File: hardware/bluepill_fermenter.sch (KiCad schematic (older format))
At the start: 1 part, among them J1 Conn_01x02

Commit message: Differentail control
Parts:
- added C1, C2, C3, C4: 100nF, symbol Device:C
- added J2: Conn_01x07, SIP7, symbol Connector_Generic:Conn_01x07
- added J3: Conn_01x03, symbol Connector_Generic:Conn_01x03
- added J4, J5: Conn_01x04, SIP4, symbol Connector_Generic:Conn_01x04
- added Q1, Q2: 2N7000, Package_TO_SOT_THT:TO-92_Inline, symbol Transistor_FET:2N7000
- added R1, R2: 1K, symbol Device:R
- added R10, R3, R4, R5, R6, R7, R8: 10K, symbol Device:R
- added R11, R12: 470R, symbol Device:R
- added R9: 50R, symbol Device:R
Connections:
- net +5V: now also J2.1 (Pin_1), J3.1 (Pin_1), R10.2
- net Bluepill Node/I2C1_SCL: now also J5.3 (Pin_3)
- net Bluepill Node/I2C1_SDA: now also J5.4 (Pin_4)
- net Bluepill Node/UART1_RX: now also J4.3 (Pin_3)
- net Bluepill Node/UART1_TX: now also J4.4 (Pin_4)
- net GNDREF: now also C1.2, C2.2, C3.1, C3.2, J2.7 (Pin_7), J4.2 (Pin_2), J5.2 (Pin_2), R5.1, R6.1, R9.2
- new net: Q1.2 (G), R1.1, R3.2
- new net: Q2.2 (G), R2.1, R4.2
- new net +3V3: J4.1 (Pin_1), J5.1 (Pin_1)
- new net COOLER_CONTROL: R1.2
- new net COOLER_INPUT: J2.5 (Pin_5), R10.1, R7.1
- new net COOLER_LED: J3.2 (Pin_2), R11.1
- new net COOLER_OUTPUT: J2.2 (Pin_2), Q1.3 (D), R11.2
- new net GNDPWR: C4.1, C4.2, J2.4 (Pin_4), Q1.1 (S), Q2.1 (S), R3.1, R4.1, R9.1
- new net HEATER_CONTROL: R2.2
- new net HEATER_INPUT: J2.6 (Pin_6), R8.1
- new net HEATER_LED: J3.3 (Pin_3), R12.1
- new net HEATER_OUTPUT: J2.3 (Pin_3), Q2.3 (D), R12.2
- new net TEMP0: C1.1, R5.2, R7.2
- new net TEMP1: C2.1, R6.2, R8.2

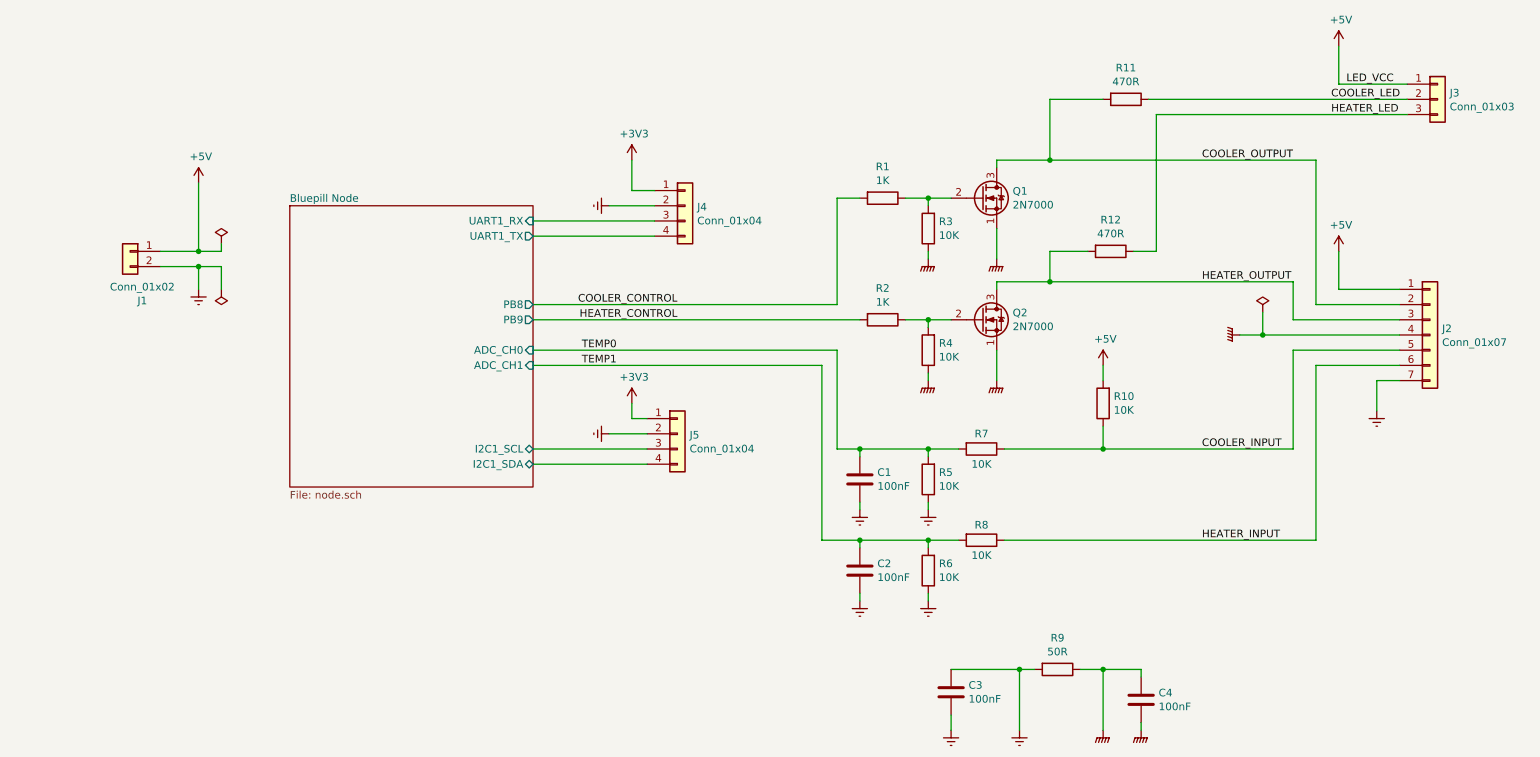
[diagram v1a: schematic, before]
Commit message: Add onboard temp sensor
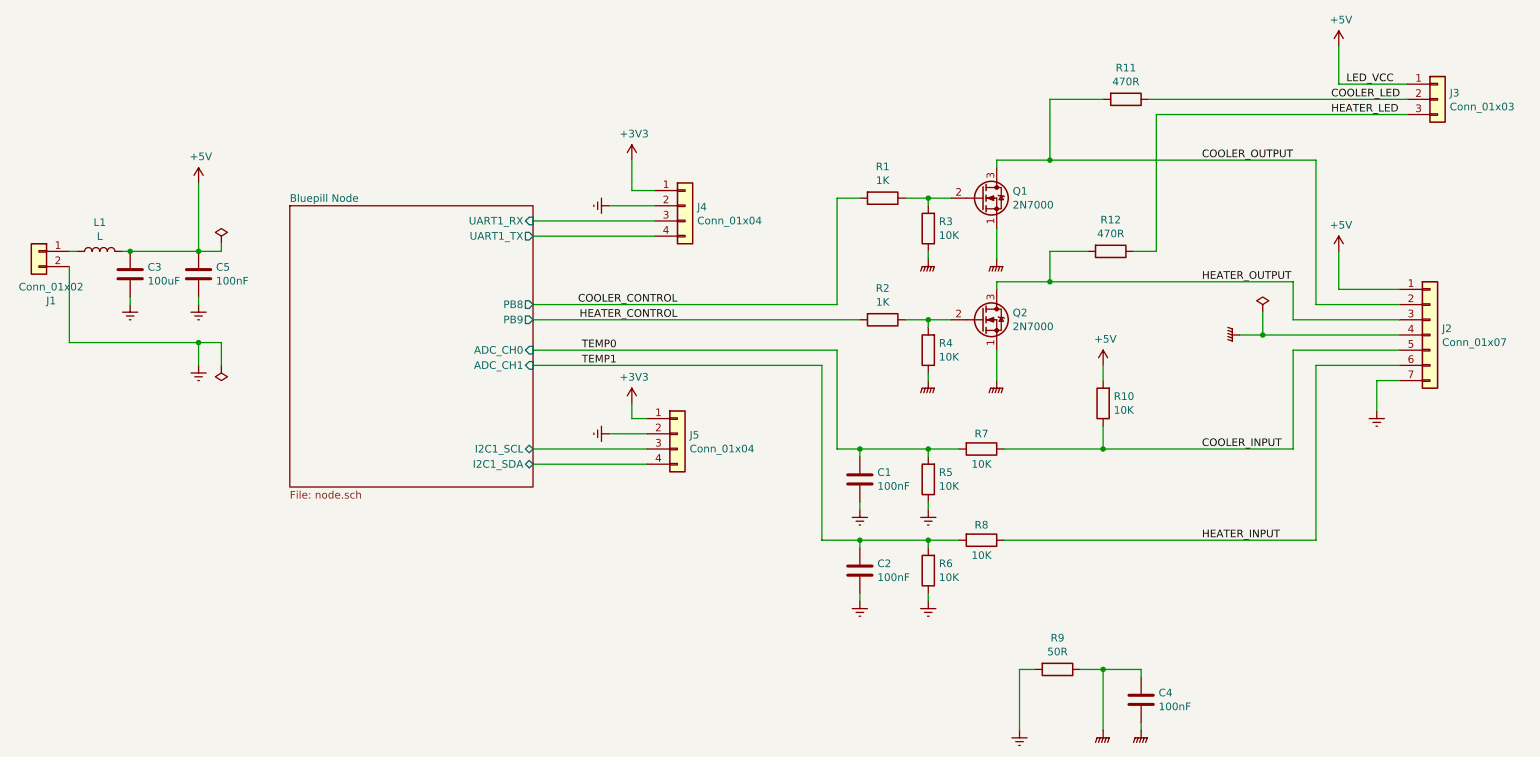
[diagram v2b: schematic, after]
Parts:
- added C5: 100nF, RA1_2, symbol Device:C
- added L1: L, AX3_2N, symbol Device:L
- C1, C2, C4: footprint (none) -> RA1_2
- C3: value 100nF -> 100uF; footprint (none) -> RA1_3
- J3: footprint (none) -> SIP3
- Q1, Q2: footprint Package_TO_SOT_THT:TO-92_Inline -> TO92
- R1, R10, R11, R12, R2, R3, R4, R5, R6, R7, R8, R9: footprint (none) -> AX2_1N
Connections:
- net +5V: now also C3.1, C5.1, L1.2; no longer J1.1 (Pin_1)
- net GNDREF: now also C5.2; no longer C3.1
- new net: J1.1 (Pin_1), L1.1
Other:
- moved on the sheet: J1
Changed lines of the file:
@@
 L Connector_Generic:Conn_01x02 J1
 U 1 1 5C14C190
-P 1700 2850
-F 0 "J1" H 1620 2525 50  0000 C CNN
-F 1 "Conn_01x02" H 1620 2616 50  0000 C CNN
-F 2 "SIP2" H 1700 2850 50  0001 C CNN
-F 3 "~" H 1700 2850 50  0001 C CNN
-	1    1700 2850
+P 1100 2850
+F 0 "J1" H 1020 2525 50  0000 C CNN
+F 1 "Conn_01x02" H 1020 2616 50  0000 C CNN
+F 2 "SIP2" H 1100 2850 50  0001 C CNN
+F 3 "~" H 1100 2850 50  0001 C CNN
+	1    1100 2850
 	-1   0    0    -1
 $EndComp
@@
 L power:GNDREF #PWR0110
 U 1 1 5C14C26C
-P 2150 3100
-F 0 "#PWR0110" H 2150 2850 50  0001 C CNN
-F 1 "GNDREF" H 2155 2927 50  0001 C CNN
-F 2 "" H 2150 3100 50  0001 C CNN
-F 3 "" H 2150 3100 50  0001 C CNN
-	1    2150 3100
-	1    0    0    -1
-$EndComp
-Wire Wire Line
-	2150 2950 2150 3100
+P 2150 3600
+F 0 "#PWR0110" H 2150 3350 50  0001 C CNN
+F 1 "GNDREF" H 2155 3427 50  0001 C CNN
+F 2 "" H 2150 3600 50  0001 C CNN
+F 3 "" H 2150 3600 50  0001 C CNN
+	1    2150 3600
+	1    0    0    -1
+$EndComp
+Wire Wire Line
+	2150 3450 2150 3600
 $Comp
 L power:PWR_FLAG #FLG0101
@@
 L power:PWR_FLAG #FLG0102
 U 1 1 5C14C309
-P 2300 3100
-F 0 "#FLG0102" H 2300 3175 50  0001 C CNN
-F 1 "PWR_FLAG" H 2300 3274 50  0001 C CNN
-F 2 "" H 2300 3100 50  0001 C CNN
-F 3 "~" H 2300 3100 50  0001 C CNN
-	1    2300 3100
+P 2300 3600
+F 0 "#FLG0102" H 2300 3675 50  0001 C CNN
+F 1 "PWR_FLAG" H 2300 3774 50  0001 C CNN
+F 2 "" H 2300 3600 50  0001 C CNN
+F 3 "~" H 2300 3600 50  0001 C CNN
+	1    2300 3600
 	-1   0    0    1
 $EndComp
 Wire Wire Line
-	2300 3100 2300 2950
-Wire Wire Line
-	2300 2950 2150 2950
-Wire Wire Line
-	1900 2850 2150 2850
-Connection ~ 2150 2850
-Wire Wire Line
-	2150 2950 1900 2950
-Connection ~ 2150 2950
+	2300 3600 2300 3450
+Wire Wire Line
+	2300 3450 2150 3450
+Wire Wire Line
+	2150 3450 1300 3450
+Connection ~ 2150 3450
 Text Label 5300 3200 2    50   ~ 0
 COOLER_CONTROL
@@
 F 0 "R7" V 7200 4150 50  0000 C CNN
 F 1 "10K" V 7400 4150 50  0000 C CNN
-F 2 "" V 7230 4150 50  0001 C CNN
+F 2 "AX2_1N" V 7230 4150 50  0001 C CNN
 F 3 "~" H 7300 4150 50  0001 C CNN
 	1    7300 4150
@@
 F 0 "R1" V 6443 2500 50  0000 C CNN
 F 1 "1K" V 6534 2500 50  0000 C CNN
-F 2 "" V 6580 2500 50  0001 C CNN
+F 2 "AX2_1N" V 6580 2500 50  0001 C CNN
 F 3 "~" H 6650 2500 50  0001 C CNN
 	1    6650 2500
@@
 F 0 "Q1" H 7505 2546 50  0000 L CNN
 F 1 "2N7000" H 7505 2455 50  0000 L CNN
-F 2 "Package_TO_SOT_THT:TO-92_Inline" H 7500 2425 50  0001 L CIN
+F 2 "TO92" H 7500 2425 50  0001 L CIN
 F 3 "https://www.fairchildsemi.com/datasheets/2N/2N7000.pdf" H 7300 2500 50  0001 L CNN
 	1    7300 2500
@@
 F 0 "Q2" H 7505 3346 50  0000 L CNN
 F 1 "2N7000" H 7505 3255 50  0000 L CNN
-F 2 "Package_TO_SOT_THT:TO-92_Inline" H 7500 3225 50  0001 L CIN
+F 2 "TO92" H 7500 3225 50  0001 L CIN
 F 3 "https://www.fairchildsemi.com/datasheets/2N/2N7000.pdf" H 7300 3300 50  0001 L CNN
 	1    7300 3300
@@
 F 0 "R2" V 6443 3300 50  0000 C CNN
 F 1 "1K" V 6534 3300 50  0000 C CNN
-F 2 "" V 6580 3300 50  0001 C CNN
+F 2 "AX2_1N" V 6580 3300 50  0001 C CNN
 F 3 "~" H 6650 3300 50  0001 C CNN
 	1    6650 3300
@@
 F 0 "R4" H 6880 3454 50  0000 R CNN
 F 1 "10K" H 6880 3545 50  0000 R CNN
-F 2 "" V 6880 3500 50  0001 C CNN
+F 2 "AX2_1N" V 6880 3500 50  0001 C CNN
 F 3 "~" H 6950 3500 50  0001 C CNN
 	1    6950 3500
@@
 F 0 "R3" H 6880 2654 50  0000 R CNN
 F 1 "10K" H 6880 2745 50  0000 R CNN
-F 2 "" V 6880 2700 50  0001 C CNN
+F 2 "AX2_1N" V 6880 2700 50  0001 C CNN
 F 3 "~" H 6950 2700 50  0001 C CNN
 	1    6950 2700
@@
 F 0 "R5" H 6880 4304 50  0000 R CNN
 F 1 "10K" H 6880 4395 50  0000 R CNN
-F 2 "" V 6880 4350 50  0001 C CNN
+F 2 "AX2_1N" V 6880 4350 50  0001 C CNN
 F 3 "~" H 6950 4350 50  0001 C CNN
 	1    6950 4350
@@
 F 0 "R8" V 7200 4750 50  0000 C CNN
 F 1 "10K" V 7400 4750 50  0000 C CNN
-F 2 "" V 7230 4750 50  0001 C CNN
+F 2 "AX2_1N" V 7230 4750 50  0001 C CNN
 F 3 "~" H 7300 4750 50  0001 C CNN
 	1    7300 4750
@@
 F 0 "R6" H 6880 4904 50  0000 R CNN
 F 1 "10K" H 6880 4995 50  0000 R CNN
-F 2 "" V 6880 4950 50  0001 C CNN
+F 2 "AX2_1N" V 6880 4950 50  0001 C CNN
 F 3 "~" H 6950 4950 50  0001 C CNN
 	1    6950 4950
@@
 F 0 "R12" V 7943 2850 50  0000 C CNN
 F 1 "470R" V 8034 2850 50  0000 C CNN
-F 2 "" V 8080 2850 50  0001 C CNN
+F 2 "AX2_1N" V 8080 2850 50  0001 C CNN
 F 3 "~" H 8150 2850 50  0001 C CNN
 	1    8150 2850
@@
 F 0 "R11" V 8043 1850 50  0000 C CNN
 F 1 "470R" V 8134 1850 50  0000 C CNN
-F 2 "" V 8180 1850 50  0001 C CNN
+F 2 "AX2_1N" V 8180 1850 50  0001 C CNN
 F 3 "~" H 8250 1850 50  0001 C CNN
 	1    8250 1850
@@
 F 0 "R10" H 8030 3804 50  0000 R CNN
 F 1 "10K" H 8030 3895 50  0000 R CNN
-F 2 "" V 8030 3850 50  0001 C CNN
+F 2 "AX2_1N" V 8030 3850 50  0001 C CNN
 F 3 "~" H 8100 3850 50  0001 C CNN
 	1    8100 3850
@@
 F 0 "R9" V 7593 5600 50  0000 C CNN
 F 1 "50R" V 7684 5600 50  0000 C CNN
-F 2 "" V 7730 5600 50  0001 C CNN
+F 2 "AX2_1N" V 7730 5600 50  0001 C CNN
 F 3 "~" H 7800 5600 50  0001 C CNN
 	1    7800 5600
@@
 F 0 "C4" H 8465 5846 50  0000 L CNN
 F 1 "100nF" H 8465 5755 50  0000 L CNN
-F 2 "" H 8388 5650 50  0001 C CNN
+F 2 "RA1_2" H 8388 5650 50  0001 C CNN
 F 3 "~" H 8350 5800 50  0001 C CNN
 	1    8350 5800
 	1    0    0    -1
 $EndComp
-$Comp
-L Device:C C3
-U 1 1 5C1574E9
-P 7100 5750
-F 0 "C3" H 7215 5796 50  0000 L CNN
-F 1 "100nF" H 7215 5705 50  0000 L CNN
-F 2 "" H 7138 5600 50  0001 C CNN
-F 3 "~" H 7100 5750 50  0001 C CNN
-	1    7100 5750
-	1    0    0    -1
-$EndComp
 Wire Wire Line
 	8100 5600 8100 6000
 Wire Wire Line
 	7550 5600 7550 6000
-$Comp
-L power:GNDREF #PWR0117
-U 1 1 5C15946D
-P 7100 6000
-F 0 "#PWR0117" H 7100 5750 50  0001 C CNN
-F 1 "GNDREF" H 7105 5827 50  0001 C CNN
-F 2 "" H 7100 6000 50  0001 C CNN
-F 3 "" H 7100 6000 50  0001 C CNN
-	1    7100 6000
-	1    0    0    -1
-$EndComp
 $Comp
 L power:GNDPWR #PWR0118
@@
 Wire Wire Line
 	7650 5600 7550 5600
-Wire Wire Line
-	7100 5600 7550 5600
-Connection ~ 7550 5600
-Wire Wire Line
-	7100 5900 7100 6000
 $Comp
 L Device:C C1
@@
 F 0 "C1" H 6615 4396 50  0000 L CNN
 F 1 "100nF" H 6615 4305 50  0000 L CNN
-F 2 "" H 6538 4200 50  0001 C CNN
+F 2 "RA1_2" H 6538 4200 50  0001 C CNN
 F 3 "~" H 6500 4350 50  0001 C CNN
 	1    6500 4350
@@
 F 0 "C2" H 6615 4996 50  0000 L CNN
 F 1 "100nF" H 6615 4905 50  0000 L CNN
-F 2 "" H 6538 4800 50  0001 C CNN
+F 2 "RA1_2" H 6538 4800 50  0001 C CNN
 F 3 "~" H 6500 4950 50  0001 C CNN
 	1    6500 4950
@@
 F 0 "J3" H 10380 1892 50  0000 L CNN
 F 1 "Conn_01x03" H 10380 1801 50  0000 L CNN
-F 2 "" H 10300 1850 50  0001 C CNN
+F 2 "SIP3" H 10300 1850 50  0001 C CNN
 F 3 "~" H 10300 1850 50  0001 C CNN
 	1    10300 1850
@@
 	9650 1750 10100 1750
 $Comp
-L power:+5V #PWR?
+L power:+5V #PWR07
 U 1 1 5C1965D5
 P 9650 2850
-F 0 "#PWR?" H 9650 2700 50  0001 C CNN
+F 0 "#PWR07" H 9650 2700 50  0001 C CNN
 F 1 "+5V" H 9665 3023 50  0000 C CNN
 F 2 "" H 9650 2850 50  0001 C CNN
@@
 Wire Wire Line
 	8400 1850 10100 1850
+$Comp
+L Device:L L1
+U 1 1 5C15915B
+P 1500 2850
+F 0 "L1" V 1690 2850 50  0000 C CNN
+F 1 "L" V 1599 2850 50  0000 C CNN
+F 2 "AX3_2N" H 1500 2850 50  0001 C CNN
+F 3 "~" H 1500 2850 50  0001 C CNN
+	1    1500 2850
+	0    -1   -1   0
+$EndComp
+Wire Wire Line
+	1300 2950 1300 3450
+$Comp
+L Device:C C3
+U 1 1 5C15D8AF
+P 1700 3000
+F 0 "C3" H 1815 3046 50  0000 L CNN
+F 1 "100uF" H 1815 2955 50  0000 L CNN
+F 2 "RA1_3" H 1738 2850 50  0001 C CNN
+F 3 "~" H 1700 3000 50  0001 C CNN
+	1    1700 3000
+	1    0    0    -1
+$EndComp
+$Comp
+L Device:C C5
+U 1 1 5C15D9F4
+P 2150 3000
+F 0 "C5" H 2265 3046 50  0000 L CNN
+F 1 "100nF" H 2265 2955 50  0000 L CNN
+F 2 "RA1_2" H 2188 2850 50  0001 C CNN
+F 3 "~" H 2150 3000 50  0001 C CNN
+	1    2150 3000
+	1    0    0    -1
+$EndComp
+Connection ~ 2150 2850
+Wire Wire Line
+	2150 2850 1700 2850
+Wire Wire Line
+	1650 2850 1700 2850
+Connection ~ 1700 2850
+$Comp
+L power:GNDREF #PWR05
+U 1 1 5C16250C
+P 1700 3200
+F 0 "#PWR05" H 1700 2950 50  0001 C CNN
+F 1 "GNDREF" H 1705 3027 50  0001 C CNN
+F 2 "" H 1700 3200 50  0001 C CNN
+F 3 "" H 1700 3200 50  0001 C CNN
+	1    1700 3200
+	1    0    0    -1
+$EndComp
+$Comp
+L power:GNDREF #PWR06
+U 1 1 5C16254B
+P 2150 3200
+F 0 "#PWR06" H 2150 2950 50  0001 C CNN
+F 1 "GNDREF" H 2155 3027 50  0001 C CNN
+F 2 "" H 2150 3200 50  0001 C CNN
+F 3 "" H 2150 3200 50  0001 C CNN
+	1    2150 3200
+	1    0    0    -1
+$EndComp
+Wire Wire Line
+	2150 3150 2150 3200
+Wire Wire Line
+	1700 3150 1700 3200
+Wire Wire Line
+	1350 2850 1300 2850
 $EndSCHEMATC

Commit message: Set point set with terminal
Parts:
- added C? (x2): 10uF, RA1_2, symbol Device:C
- added R?: 2K4, AX2_1N, symbol Device:R
- R10: value 10K -> 2K4
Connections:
- net +5V: now also R?.2
- net GNDREF: now also C?.2, C?.2
- net HEATER_INPUT: now also R?.1
- net TEMP0: now also C?.1
- net TEMP1: now also C?.1
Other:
- moved on the sheet: R10
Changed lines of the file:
@@
 	6950 4150 6500 4150
 Wire Wire Line
-	6350 4150 6350 3500
-Wire Wire Line
-	4350 3500 6350 3500
+	6000 4150 6000 3500
+Wire Wire Line
+	4350 3500 6000 3500
 Connection ~ 6950 4150
 Wire Wire Line
-	6250 3600 6250 4750
-Wire Wire Line
-	6250 4750 6500 4750
-Wire Wire Line
-	4350 3600 6250 3600
+	5600 3600 5600 4750
+Wire Wire Line
+	5600 4750 6000 4750
+Wire Wire Line
+	4350 3600 5600 3600
 Wire Wire Line
 	6950 4800 6950 4750
@@
 L Device:R R10
 U 1 1 5C15382B
-P 8100 3850
-F 0 "R10" H 8030 3804 50  0000 R CNN
-F 1 "10K" H 8030 3895 50  0000 R CNN
-F 2 "AX2_1N" V 8030 3850 50  0001 C CNN
-F 3 "~" H 8100 3850 50  0001 C CNN
-	1    8100 3850
+P 8100 3950
+F 0 "R10" H 8030 3904 50  0000 R CNN
+F 1 "2K4" H 8030 3995 50  0000 R CNN
+F 2 "AX2_1N" V 8030 3950 50  0001 C CNN
+F 3 "~" H 8100 3950 50  0001 C CNN
+	1    8100 3950
 	-1   0    0    1
 $EndComp
 Wire Wire Line
-	8100 4000 8100 4150
+	8100 4100 8100 4150
 Connection ~ 8100 4150
 $Comp
 L power:+5V #PWR0113
 U 1 1 5C1540C1
-P 8100 3600
-F 0 "#PWR0113" H 8100 3450 50  0001 C CNN
-F 1 "+5V" H 8115 3773 50  0000 C CNN
-F 2 "" H 8100 3600 50  0001 C CNN
-F 3 "" H 8100 3600 50  0001 C CNN
-	1    8100 3600
-	1    0    0    -1
-$EndComp
-Wire Wire Line
-	8100 3600 8100 3700
+P 8100 3750
+F 0 "#PWR0113" H 8100 3600 50  0001 C CNN
+F 1 "+5V" H 8200 3850 50  0000 C CNN
+F 2 "" H 8100 3750 50  0001 C CNN
+F 3 "" H 8100 3750 50  0001 C CNN
+	1    8100 3750
+	1    0    0    -1
+$EndComp
+Wire Wire Line
+	8100 3750 8100 3800
 $Comp
 L power:+5V #PWR0114
@@
 Connection ~ 6500 4150
 Wire Wire Line
-	6500 4150 6350 4150
+	6500 4150 6000 4150
 Wire Wire Line
 	9650 3100 10050 3100
@@
 	9500 3600 9500 4750
 Wire Wire Line
-	7450 4750 9500 4750
+	7450 4750 8100 4750
 $Comp
 L Connector_Generic:Conn_01x07 J2
@@
 P 5300 4050
 F 0 "J5" H 5380 4042 50  0000 L CNN
-F 1 "Conn_01x04" H 5380 3951 50  0000 L CNN
+F 1 "Conn_01x04" H 5380 3951 50  0001 L CNN
 F 2 "SIP4" H 5300 4050 50  0001 C CNN
 F 3 "~" H 5300 4050 50  0001 C CNN
@@
 Wire Wire Line
 	1350 2850 1300 2850
+$Comp
+L Device:C C?
+U 1 1 5C18B18D
+P 6000 4950
+F 0 "C?" H 6115 4996 50  0000 L CNN
+F 1 "10uF" H 6115 4905 50  0000 L CNN
+F 2 "RA1_2" H 6038 4800 50  0001 C CNN
+F 3 "~" H 6000 4950 50  0001 C CNN
+	1    6000 4950
+	1    0    0    -1
+$EndComp
+$Comp
+L Device:C C?
+U 1 1 5C18DA66
+P 6000 4350
+F 0 "C?" H 6115 4396 50  0000 L CNN
+F 1 "10uF" H 6115 4305 50  0000 L CNN
+F 2 "RA1_2" H 6038 4200 50  0001 C CNN
+F 3 "~" H 6000 4350 50  0001 C CNN
+	1    6000 4350
+	1    0    0    -1
+$EndComp
+$Comp
+L power:GNDREF #PWR?
+U 1 1 5C18DACC
+P 6000 5150
+F 0 "#PWR?" H 6000 4900 50  0001 C CNN
+F 1 "GNDREF" H 6005 4977 50  0001 C CNN
+F 2 "" H 6000 5150 50  0001 C CNN
+F 3 "" H 6000 5150 50  0001 C CNN
+	1    6000 5150
+	1    0    0    -1
+$EndComp
+$Comp
+L power:GNDREF #PWR?
+U 1 1 5C18DB5E
+P 6000 4550
+F 0 "#PWR?" H 6000 4300 50  0001 C CNN
+F 1 "GNDREF" H 6005 4377 50  0001 C CNN
+F 2 "" H 6000 4550 50  0001 C CNN
+F 3 "" H 6000 4550 50  0001 C CNN
+	1    6000 4550
+	1    0    0    -1
+$EndComp
+Wire Wire Line
+	6000 4500 6000 4550
+Wire Wire Line
+	6000 5100 6000 5150
+Wire Wire Line
+	6000 4800 6000 4750
+Connection ~ 6000 4750
+Wire Wire Line
+	6000 4750 6500 4750
+Wire Wire Line
+	6000 4150 6000 4200
+Connection ~ 6000 4150
+$Comp
+L Device:R R?
+U 1 1 5C19B067
+P 8100 4550
+F 0 "R?" H 8030 4504 50  0000 R CNN
+F 1 "2K4" H 8030 4595 50  0000 R CNN
+F 2 "AX2_1N" V 8030 4550 50  0001 C CNN
+F 3 "~" H 8100 4550 50  0001 C CNN
+	1    8100 4550
+	-1   0    0    1
+$EndComp
+$Comp
+L power:+5V #PWR?
+U 1 1 5C1A0A02
+P 8100 4350
+F 0 "#PWR?" H 8100 4200 50  0001 C CNN
+F 1 "+5V" H 8200 4450 50  0000 C CNN
+F 2 "" H 8100 4350 50  0001 C CNN
+F 3 "" H 8100 4350 50  0001 C CNN
+	1    8100 4350
+	1    0    0    -1
+$EndComp
+Wire Wire Line
+	8100 4350 8100 4400
+Wire Wire Line
+	8100 4700 8100 4750
+Connection ~ 8100 4750
+Wire Wire Line
+	8100 4750 9500 4750
 $EndSCHEMATC
